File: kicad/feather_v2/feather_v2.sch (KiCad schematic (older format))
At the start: 8 parts, among them P1 Maniacal Labs, P10 WyoLum, P2 Screw, P3 Screw, P6 Input, P7 Output, P8 Feather_M0

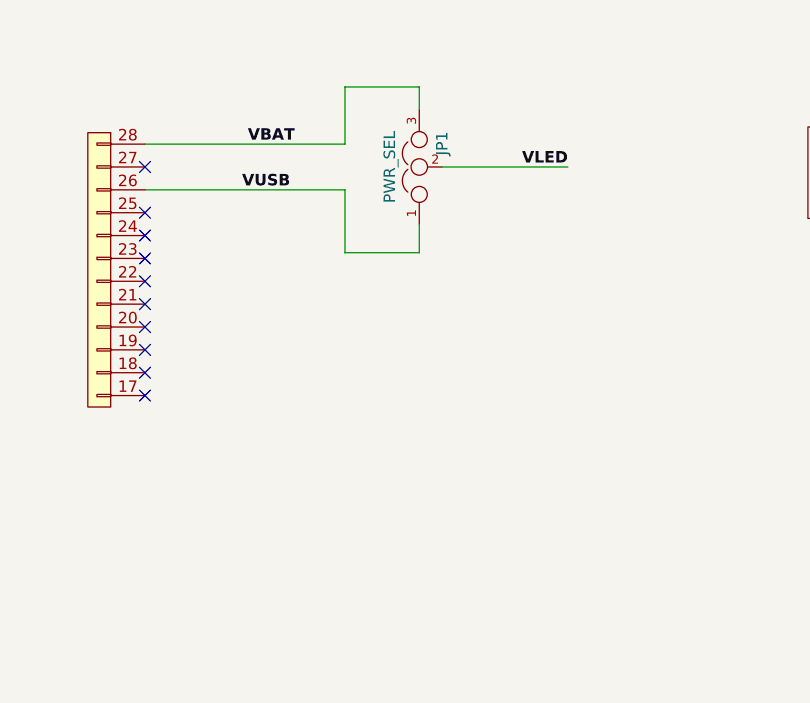
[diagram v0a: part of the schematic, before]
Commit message: feather_v2 added SMD shorting links and extra power switch
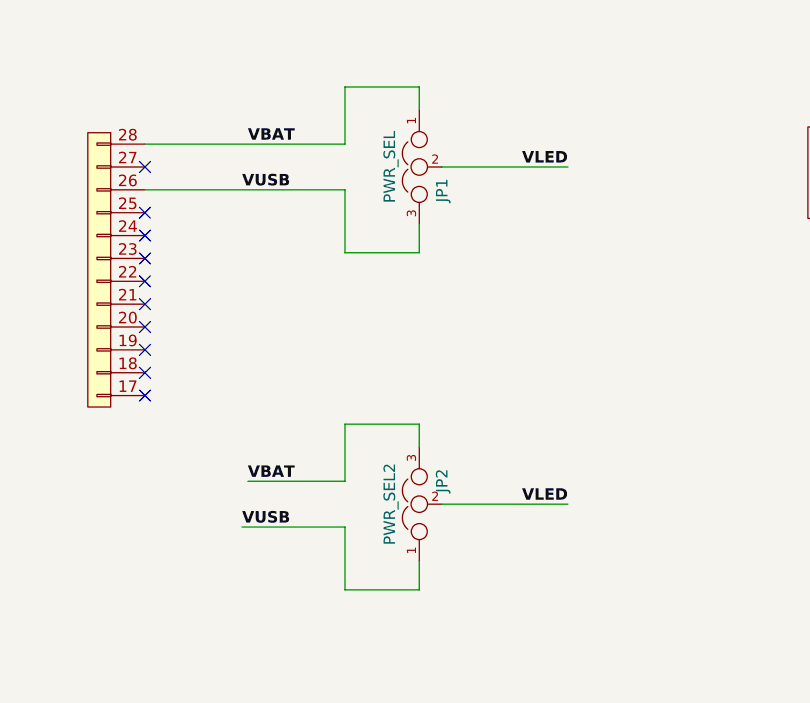
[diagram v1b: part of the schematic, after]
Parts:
- added JP2: PWR_SEL2, feather_v2:switch_spdt, symbol JUMPER3
- JP1: footprint feather_v2:Pin_Header_Straight_1x03 -> feather_v2:switch_spdt
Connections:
- net VBAT: now also JP1.1, JP2.3; no longer JP1.3
- net VLED: now also JP2.2
- net VUSB: now also JP1.3, JP2.1; no longer JP1.1
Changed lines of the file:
@@
 F 0 "JP1" H 5175 1375 50  0000 L CNN
 F 1 "PWR_SEL" H 5125 1575 50  0000 C BNN
-F 2 "feather_v2:Pin_Header_Straight_1x03" H 5125 1475 50  0001 C CNN
+F 2 "feather_v2:switch_spdt" H 5125 1475 50  0001 C CNN
 F 3 "" H 5125 1475 50  0000 C CNN
 	1    5125 1475
-	0    -1   -1   0
+	0    -1   1    0
 $EndComp
 Wire Wire Line
@@
 Text Label 4350 1575 0    50   ~ 10
 VUSB
+Wire Wire Line
+	4375 2850 4800 2850
+$Comp
+L JUMPER3 JP2
+U 1 1 586BC487
+P 5125 2950
+F 0 "JP2" H 5175 2850 50  0000 L CNN
+F 1 "PWR_SEL2" H 5125 3050 50  0000 C BNN
+F 2 "feather_v2:switch_spdt" H 5125 2950 50  0001 C CNN
+F 3 "" H 5125 2950 50  0000 C CNN
+	1    5125 2950
+	0    -1   -1   0
+$EndComp
+Wire Wire Line
+	4350 3050 4800 3050
+Text Label 5775 2950 2    50   ~ 10
+VLED
+Wire Wire Line
+	4800 2850 4800 2600
+Wire Wire Line
+	4800 2600 5125 2600
+Wire Wire Line
+	5125 2600 5125 2700
+Wire Wire Line
+	4800 3050 4800 3325
+Wire Wire Line
+	4800 3325 5125 3325
+Wire Wire Line
+	5125 3325 5125 3200
+Wire Wire Line
+	5775 2950 5225 2950
+Text Label 4375 2850 0    50   ~ 10
+VBAT
+Text Label 4350 3050 0    50   ~ 10
+VUSB
 $EndSCHEMATC

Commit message: clean up of all kicad project folders
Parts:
- removed P1: Maniacal Labs, feather_v2:logo_MLlabs_small, symbol LOGO_1
- removed P10: WyoLum, feather_v2:logo_wyo_butterfly_small, symbol LOGO_1
- added L1: LOGO_WL, feather_v2:logo_wyo_butterfly_small, symbol LOGO_WL
- added L2: LOGO_ML, feather_v2:logo_MLlabs_small, symbol LOGO_ML
- added L3: OSHW, feather_v2:OSHW_6mm, symbol OSHW
- M1: renamed from P2; symbol CONN_1 -> MTG_1
- M2: renamed from P3; symbol CONN_1 -> MTG_1
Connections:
- no-connect marks 27 -> 25
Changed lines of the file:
@@
 LIBS:feather_v2
 LIBS:ultim8x8_sym
+LIBS:ultim_bus
 LIBS:feather_v2-cache
 EELAYER 25 0
@@
 $EndDescr
 $Comp
-L CONN_1 P3
+L MTG_1 M2
 U 1 1 58151907
-P 1125 3150
-F 0 "P3" H 1205 3150 40  0000 L CNN
-F 1 "Screw" H 1125 3205 30  0001 C CNN
-F 2 "feather_v2:Screw_NPTH" H 1125 3150 60  0001 C CNN
-F 3 "" H 1125 3150 60  0000 C CNN
-F 4 "mfr_pn" H 1125 3150 60  0001 C CNN "manf#"
-	1    1125 3150
+P 7600 5775
+F 0 "M2" H 7700 5725 40  0000 L CNN
+F 1 "Screw" H 7600 5830 30  0001 C CNN
+F 2 "feather_v2:Screw_NPTH" H 7600 5775 60  0001 C CNN
+F 3 "" H 7600 5775 60  0000 C CNN
+F 4 "mfr_pn" H 7600 5775 60  0001 C CNN "manf#"
+	1    7600 5775
 	-1   0    0    1
 $EndComp
@@
 	2375 2075 2750 2075
 $Comp
-L LOGO_1 P1
-U 1 1 581524CC
-P 1000 3450
-F 0 "P1" H 950 3550 40  0000 L CNN
-F 1 "Maniacal Labs" H 1000 3505 30  0001 C CNN
-F 2 "feather_v2:logo_MLlabs_small" H 1800 3450 60  0000 C CNN
-F 3 "" H 1000 3450 60  0000 C CNN
-	1    1000 3450
-	1    0    0    -1
-$EndComp
-$Comp
-L LOGO_1 P10
-U 1 1 58152670
-P 1000 3675
-F 0 "P10" H 950 3775 40  0000 L CNN
-F 1 "WyoLum" H 1000 3730 30  0001 C CNN
-F 2 "feather_v2:logo_wyo_butterfly_small" H 1950 3675 60  0000 C CNN
-F 3 "" H 1000 3675 60  0000 C CNN
-	1    1000 3675
-	1    0    0    -1
-$EndComp
-$Comp
-L CONN_1 P2
+L MTG_1 M1
 U 1 1 58152AF0
-P 1125 2950
-F 0 "P2" H 1205 2950 40  0000 L CNN
-F 1 "Screw" H 1125 3005 30  0001 C CNN
-F 2 "feather_v2:Screw_NPTH" H 1125 2950 60  0001 C CNN
-F 3 "" H 1125 2950 60  0000 C CNN
-F 4 "mfr_pn" H 1125 2950 60  0001 C CNN "manf#"
-	1    1125 2950
+P 7600 5450
+F 0 "M1" H 7700 5400 40  0000 L CNN
+F 1 "Screw" H 7600 5505 30  0001 C CNN
+F 2 "feather_v2:Screw_NPTH" H 7600 5450 60  0001 C CNN
+F 3 "" H 7600 5450 60  0000 C CNN
+F 4 "mfr_pn" H 7600 5450 60  0001 C CNN "manf#"
+	1    7600 5450
 	-1   0    0    1
 $EndComp
@@
 	1    0    0    -1
 $EndComp
-NoConn ~ 1275 3150
-NoConn ~ 1275 2950
 $Comp
 L CONN4_S P6
@@
 Wire Wire Line
 	5775 1475 5225 1475
-Text Notes 1350 3050 0    50   ~ 0
+Text Notes 7350 5250 0    50   ~ 0
 Mounting Holes
 Text Label 4375 1375 0    50   ~ 10
@@
 Text Label 4350 3050 0    50   ~ 10
 VUSB
+$Comp
+L LOGO_ML L2
+U 1 1 58E27187
+P 10050 6225
+F 0 "L2" H 10050 5950 40  0000 C CNN
+F 1 "LOGO_ML" H 10050 6408 60  0001 C CNN
+F 2 "feather_v2:logo_MLlabs_small" H 10050 6225 60  0001 C CNN
+F 3 "" H 10050 6225 60  0001 C CNN
+F 4 "mfr_pn" H 10050 6225 60  0001 C CNN "manf#"
+	1    10050 6225
+	1    0    0    -1
+$EndComp
+$Comp
+L LOGO_WL L1
+U 1 1 58E271AD
+P 9625 6325
+F 0 "L1" H 9625 6150 40  0000 C CNN
+F 1 "LOGO_WL" H 9625 6461 60  0001 C CNN
+F 2 "feather_v2:logo_wyo_butterfly_small" H 9625 6325 60  0001 C CNN
+F 3 "" H 9625 6325 60  0001 C CNN
+F 4 "mfr_pn" H 9625 6325 60  0001 C CNN "manf#"
+	1    9625 6325
+	1    0    0    -1
+$EndComp
+$Comp
+L OSHW L3
+U 1 1 58E271D3
+P 10700 6075
+F 0 "L3" H 10700 5650 40  0000 C CNN
+F 1 "OSHW" H 10700 6175 40  0001 C CNN
+F 2 "feather_v2:OSHW_6mm" H 10700 6075 60  0001 C CNN
+F 3 "" H 10700 6075 60  0000 C CNN
+F 4 "mfr_pn" H 10700 6075 60  0001 C CNN "manf#"
+	1    10700 6075
+	1    0    0    -1
+$EndComp
 $EndSCHEMATC
